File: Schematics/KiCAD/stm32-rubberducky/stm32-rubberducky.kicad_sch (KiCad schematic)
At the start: 23 parts, among them J1 USB_A, J2 USART, J3 Micro_SD_Card, U1 STM32F103C6T6, U2 UA78L033AIPKR2, Y1 LFXTAL033863Reel

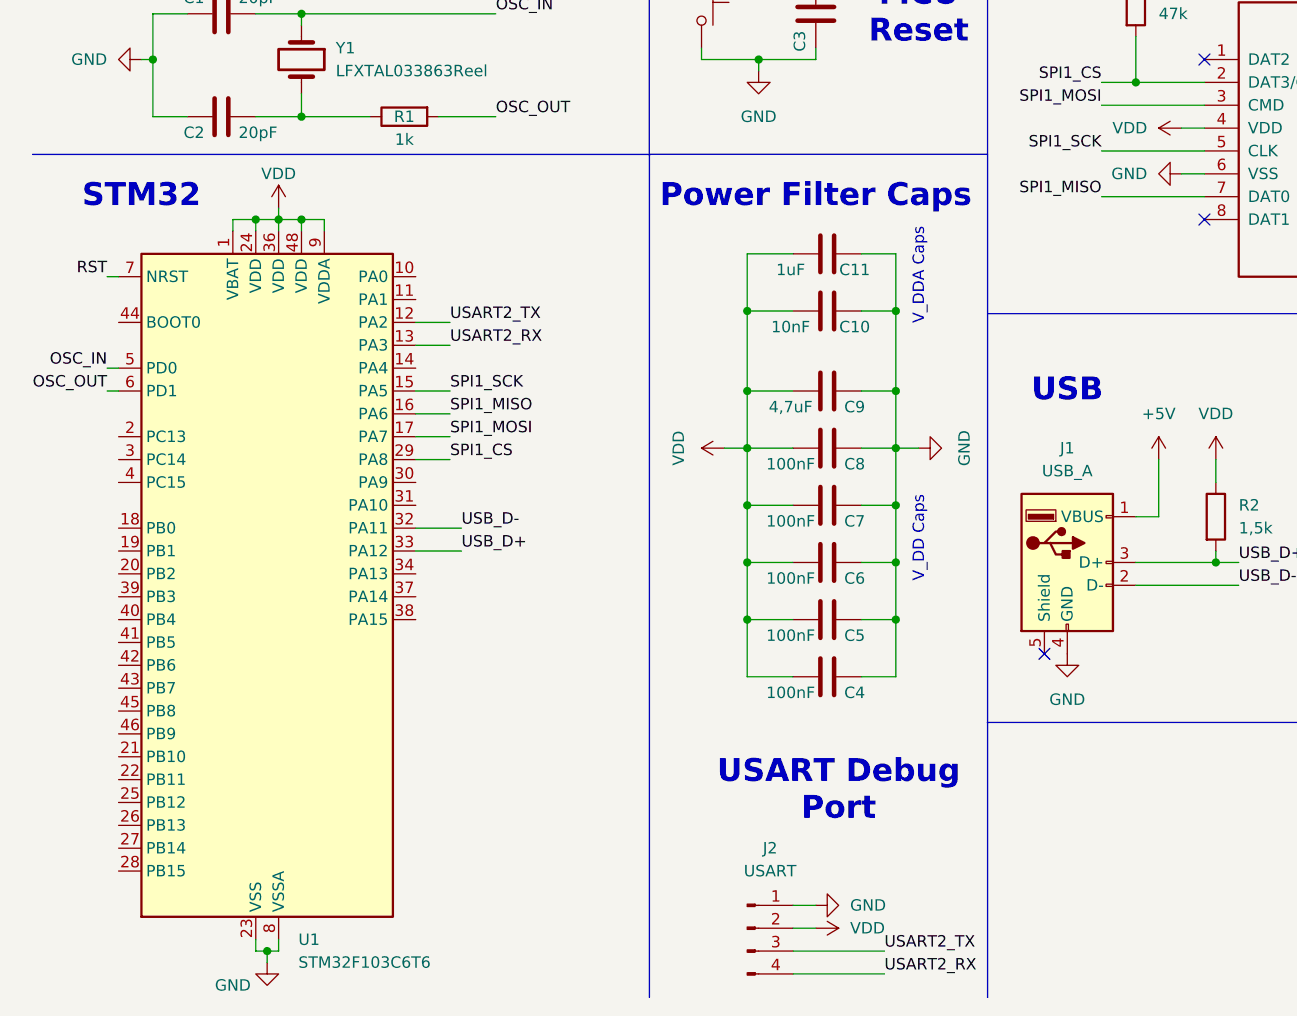
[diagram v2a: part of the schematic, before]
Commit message: finished schematic and added it to the documentation Readme
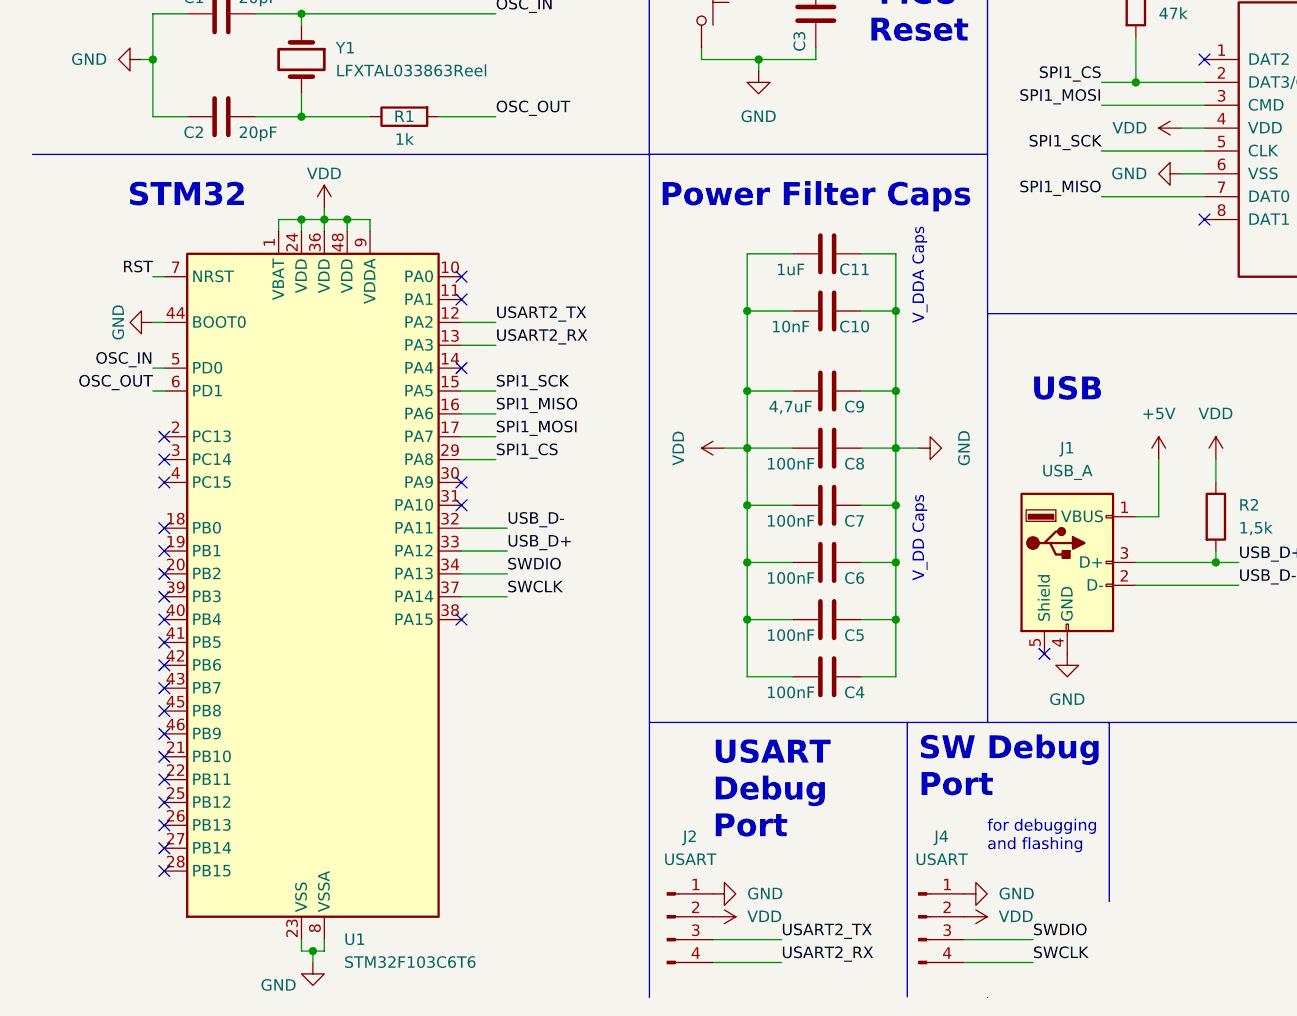
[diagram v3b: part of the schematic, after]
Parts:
- added J4: USART, symbol Connector:Conn_01x04_Pin
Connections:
- net GND: now also U1.44 (BOOT0), J4.1 (Pin_1)
- net VDD: now also J4.2 (Pin_2)
- net SWDIO: now reaches U1.34 (PA13)
- net SWDIO: now also J4.3 (Pin_3)
- net SWCLK: now reaches U1.37 (PA14)
- net SWCLK: now also J4.4 (Pin_4)
- no-connect marks 4 -> 29
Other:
- note added: "SW Debug Port"
- note added: "for debugging and flashing"
- title: (none) -> STM32 Rubber Ducky
- moved on the sheet: J2, U1
